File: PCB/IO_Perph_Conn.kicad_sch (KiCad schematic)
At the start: 1 part, among them U2 STM32MP157FABx

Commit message: PCB_UPDATE
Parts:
- removed U2: STM32MP157FABx, Package_BGA:ST_LFBGA-354_16x16mm_Layout19x19_P0.8mm, symbol New_Library:STM32MP157FABx
- added U2: STM32MP157FABx, Package_BGA:ST_LFBGA-354_16x16mm_Layout19x19_P0.8mm, symbol New_Library:STM32MP157FABx
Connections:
- new net SDMMC1_CK: U2.C10 (PC12)
- new net SDMMC1_CMD: U2.B10 (PD2)
- new net SDMMC1_D0: U2.C11 (PC8)
- new net SDMMC1_D1: U2.A10 (PC9)
- new net SDMMC1_D2: U2.D11 (PC10)
- new net SDMMC1_D3: U2.A11 (PC11)
- new net uSD_DETECT: U2.B5 (PB7)
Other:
- removed sheet DDR
- removed sheet FLASH_SD
- removed sheet IO_Perph_Conn
- removed sheet MPU_PWR
- removed sheet PWR
- removed sheet RCC_BOOT_RST_DEBUG

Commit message: Look like MPU done
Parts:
- added D2: LED_R, LED_SMD:LED_0402_1005Metric, symbol Device:LED
- added D3: LED_B, LED_SMD:LED_0402_1005Metric, symbol Device:LED
- added R43, R44: ~, symbol Device:R
- added TP14, TP15: TestPoint, TestPoint:TestPoint_Pad_D1.0mm, symbol Connector:TestPoint
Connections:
- net at U2.P2 (PA13): now also D2.1 (K), TP14.1
- net at U2.R1 (PA14): now also D3.1 (K), TP15.1
- new net: D3.2 (A), R43.1
- new net: D2.2 (A), R44.1
- new net 3V3: R43.2, R44.2

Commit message: PCB_UPDATE
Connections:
- net NAND_D4: now reaches U2.T10 (PE7)
- net NAND_D5: now reaches U2.T11 (PE8)
- net NAND_NCE: now reaches U2.T14 (PG9)
- net NAND_D7: now reaches U2.V10 (PE10)
- net UART4_TX_STM: now reaches U2.V6 (PG11)
- net NAND_D6: now reaches U2.W7 (PE9)
- net NAND_D2: now reaches U2.A3 (PD0)
- net NAND_D3: now reaches U2.A4 (PD1)
- net NAND_NOE: now reaches U2.D6 (PD4)
- net NAND_NWE: now reaches U2.D7 (PD5)
- net NAND_NWAIT: now reaches U2.E3 (PD6)
- net NAND_D0: now reaches U2.F3 (PD14)
- net NAND_D1: now reaches U2.G1 (PD15)
- net UART4_RX_STM: now reaches U2.T13 (PB2)
- net NAND_ALE: now reaches U2.U11 (PD12)
- net NAND_CLE: now reaches U2.V8 (PD11)

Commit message: PCB_UPDATE
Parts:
- added C114, C115: 6.8pF, Capacitor_SMD:C_0402_1005Metric, symbol Device:C
- added C116: 10nF, Capacitor_SMD:C_0402_1005Metric, symbol Device:C
- added D8: PTVS3V3S1UR, PTVS3V3S1UR:TVS_PTVS3V3S1UR, symbol PTVS3V3S1UR:PTVS3V3S1UR
- added R60, R61: 4k7, Resistor_SMD:R_0402_1005Metric, symbol Device:R
- added R63: 10k, Resistor_SMD:R_0402_1005Metric, symbol Device:R
- added S4: PTS525SM15SMTR2LFS, lib:SW_PTS525SM15SMTR2LFS, symbol PTS525SM15SMTR2LFS:PTS525SM15SMTR2LFS
- added Y2: NX2012SA-32.768K, lib:XTAL_NX2012SA-32.768K-STD-MUB-1, symbol NX2012SA-32.768K-STD-MUB-1:NX2012SA-32.768K-STD-MUB-1
- R43, R44: footprint (none) -> Resistor_SMD:R_0402_1005Metric
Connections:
- net at U2.H1 (PC14): now also C114.2, Y2.2
- net at U2.H2 (PC15): now also C115.1, Y2.1
- net PMIC_PA0_WKUP_INTR: now reaches U2.R3 (PA0)
- net SYS_I2C_SCL: now reaches U2.T12 (PB6)
- net SYS_I2C_SCL: now also R60.1
- net SYS_I2C_SDA: now reaches U2.U12 (PD13)
- net SYS_I2C_SDA: now also R61.1
- net EXT_WKUP: now reaches U2.U4 (PA1)
- net EXT_WKUP: now also C116.2, D8.C, R63.1, S4.3, S4.4
- new net GND: C114.1, C115.2, C116.1, D8.A, S4.1, S4.2
- new net VDD: R60.2, R61.2, R63.2

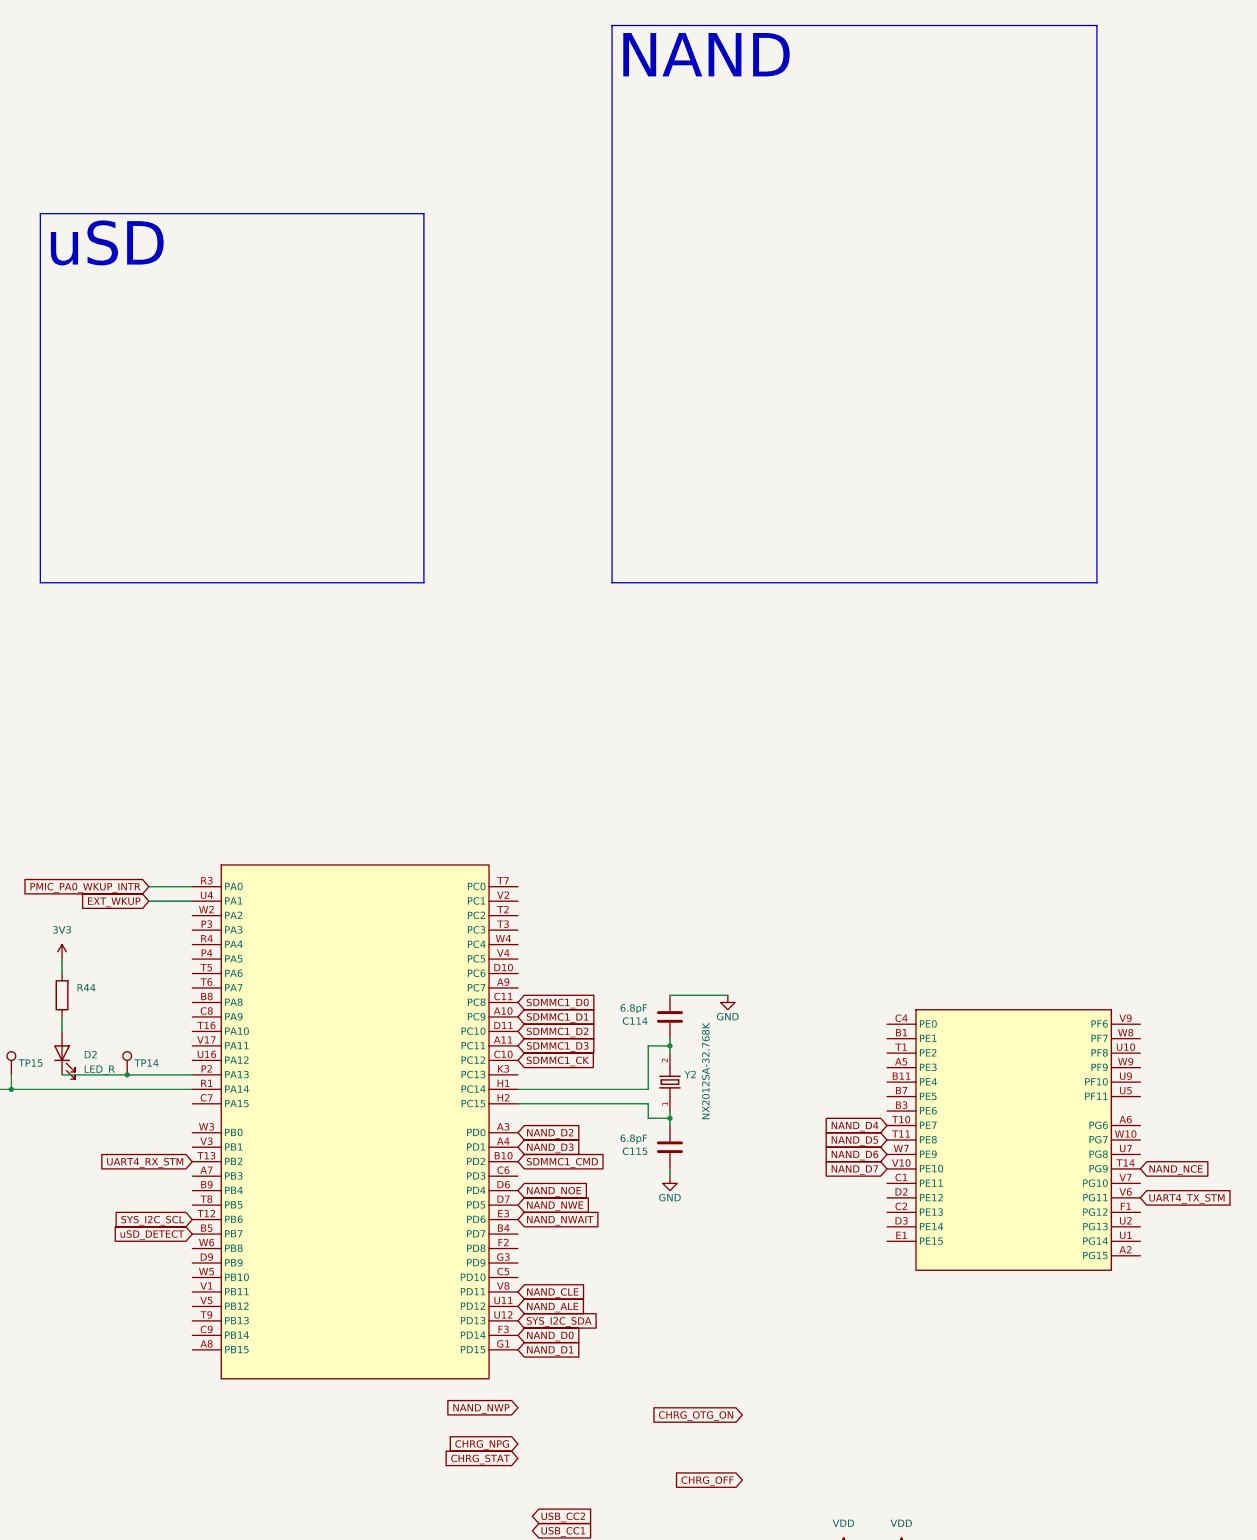
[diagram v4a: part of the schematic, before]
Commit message: added eMMC
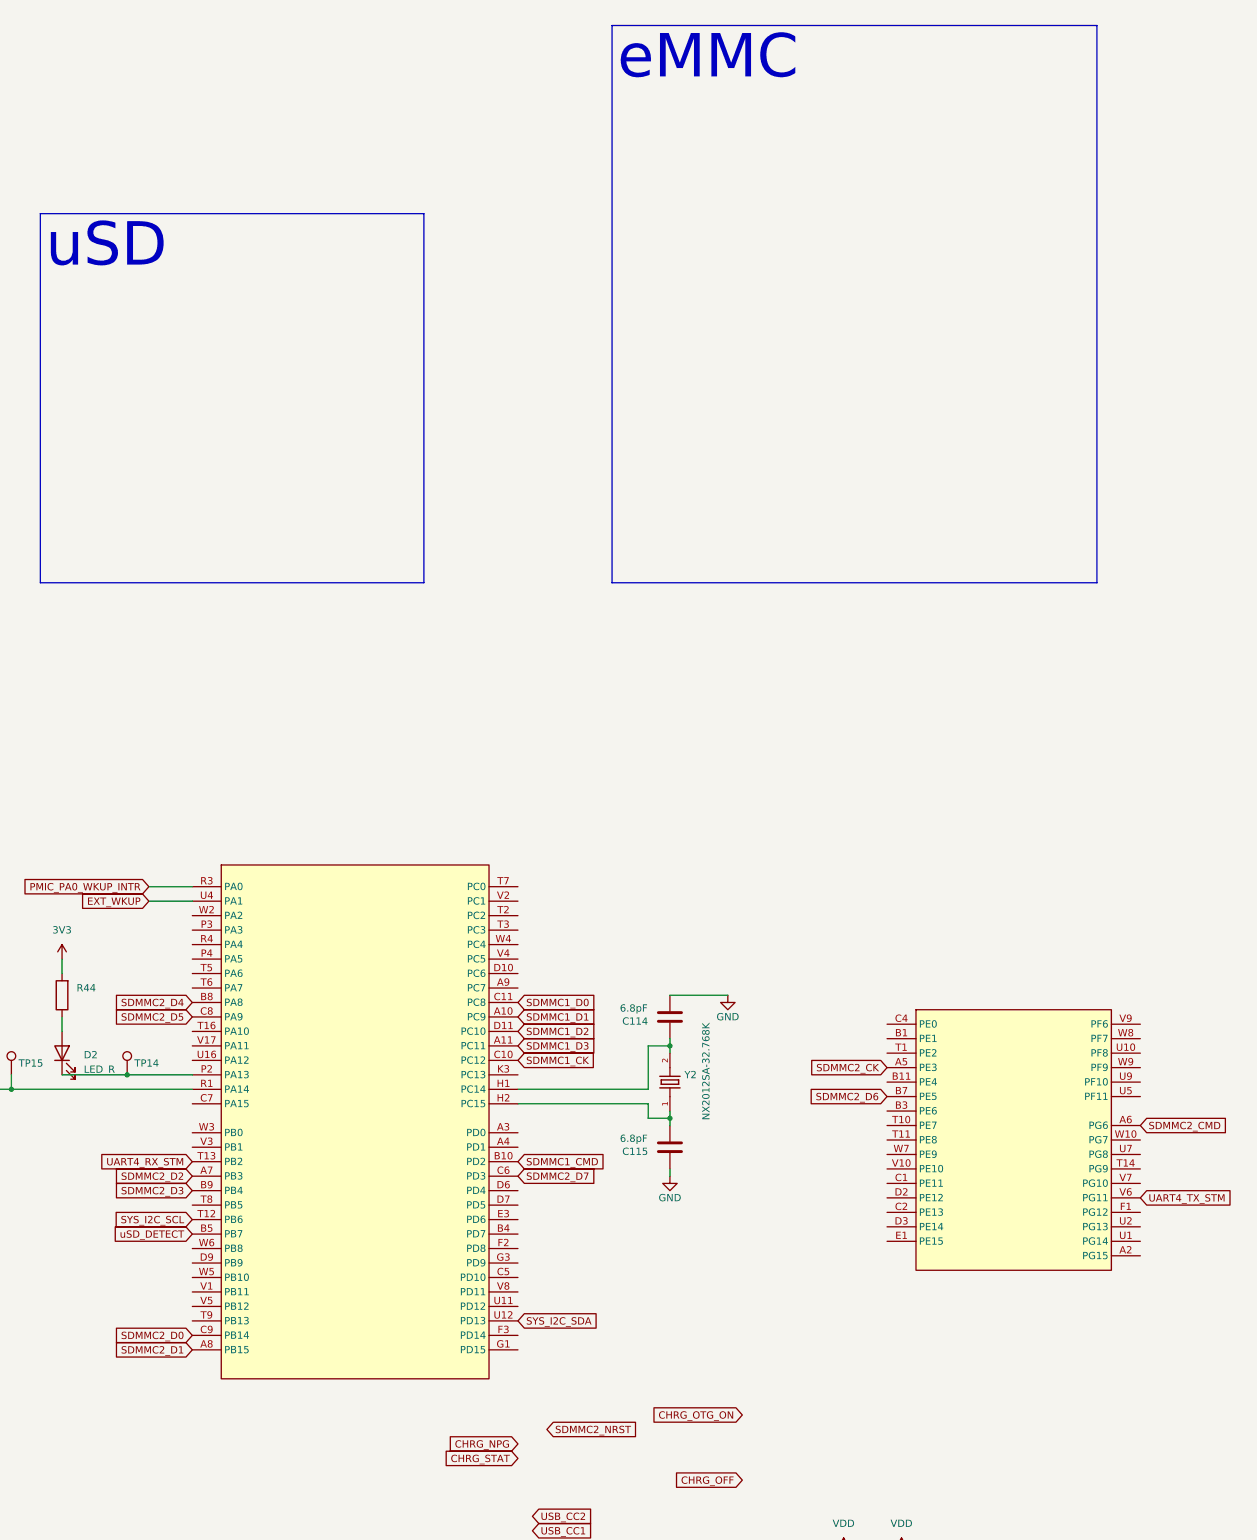
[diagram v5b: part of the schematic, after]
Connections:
- net SDMMC2_CK: now reaches U2.A5 (PE3)
- net SDMMC2_CMD: now reaches U2.A6 (PG6)
- net SDMMC2_D6: now reaches U2.B7 (PE5)
- net SDMMC2_D2: now reaches U2.A7 (PB3)
- net SDMMC2_D1: now reaches U2.A8 (PB15)
- net SDMMC2_D4: now reaches U2.B8 (PA8)
- net SDMMC2_D3: now reaches U2.B9 (PB4)
- net SDMMC2_D7: now reaches U2.C6 (PD3)
- net SDMMC2_D5: now reaches U2.C8 (PA9)
- net SDMMC2_D0: now reaches U2.C9 (PB14)
- net NAND_ALE: no longer names the net of U2.U11 (PD12)
- net NAND_CLE: no longer names the net of U2.V8 (PD11)
- net NAND_D0: no longer names the net of U2.F3 (PD14)
- net NAND_D1: no longer names the net of U2.G1 (PD15)
- net NAND_D2: no longer names the net of U2.A3 (PD0)
- net NAND_D3: no longer names the net of U2.A4 (PD1)
- net NAND_D4: no longer names the net of U2.T10 (PE7)
- net NAND_D5: no longer names the net of U2.T11 (PE8)
- net NAND_D6: no longer names the net of U2.W7 (PE9)
- net NAND_D7: no longer names the net of U2.V10 (PE10)
- net NAND_NCE: no longer names the net of U2.T14 (PG9)
- net NAND_NOE: no longer names the net of U2.D6 (PD4)
- net NAND_NWAIT: no longer names the net of U2.E3 (PD6)
- net NAND_NWE: no longer names the net of U2.D7 (PD5)

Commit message: wifi done
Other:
- note added: "RECHECK ALL PINS"
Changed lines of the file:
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@@
 		(comment 1 "Author: Mykola Grodskyi")
+	)
+	(text "RECHECK ALL PINS"
+		(exclude_from_sim no)
+		(at 127.762 -36.322 0)
+		(effects
+			(font
+				(size 12.7 12.7)
+				(thickness 2.54)
+				(bold yes)
+				(color 255 6 19 1)
+			)
+		)
+	)
+	(text "RECHECK ALL PINS"
+		(exclude_from_sim no)
+		(at 137.922 93.98 0)
+		(effects
+			(font
+				(size 12.7 12.7)
+				(thickness 2.54)
+				(bold yes)
+				(color 255 6 19 1)
+			)
+		)
+	)
+	(text "RECHECK ALL PINS"
+		(exclude_from_sim no)
+		(at -81.534 -47.498 0)
+		(effects
+			(font
+				(size 12.7 12.7)
+				(thickness 2.54)
+				(bold yes)
+				(color 255 6 19 1)
+			)
+		)
 	)
 	(text_box "I2S3 BL\n\n"
